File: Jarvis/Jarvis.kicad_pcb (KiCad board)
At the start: 4 copper layers, 30 x 55.1 mm, 134 parts, among them IC1 ADP1607, IC2 MAX-8Q, IC3 MPU-9250, IC4 STM32F411CxUx, IC5 Si4460, IC6 MS5611-01BA03, IC7 S25FL127S, J1 PYRO, J2 PWR, J3 ARM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

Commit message: Modified radio circuit to 868MHz and generated stickerBOM
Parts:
- C23: value 5.1pF -> 3pF
- C24: value 2.7pF -> 1.2pF
- C25: value 18pF -> 33pF
- C26, C28: value 8.2pF -> 5.1pF
- C27: value 15pF -> 10pF
- L2: value 56nH -> 18nH
- L3: value 56nH -> 22nH
- L4, L5: value 18nH -> 6.8nH
- L6: value 56nH -> 8.2nH
- L7: value 220nH -> 120nH
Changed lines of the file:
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@@
-(kicad_pcb (version 4) (host pcbnew 4.0.2-4+6225~38~ubuntu14.04.1-stable)
+(kicad_pcb (version 4) (host pcbnew 4.0.2+e4-6225~38~ubuntu14.04.1-stable)
   (general
-    (links 308)
-    (no_connects 0)
-    (area 81.675 72.611 117.344048 131.975)
+    (links 342)
+    (no_connects 24)
+    (area 84.924998 74.924999 115.075001 130.175002)
     (thickness 1.6)
     (drawings 164)
@@
     (45 Margin user hide)
     (46 B.CrtYd user hide)
-    (47 F.CrtYd user hide)
+    (47 F.CrtYd user)
     (48 B.Fab user hide)
     (49 F.Fab user hide)
@@
     (pad_to_mask_clearance 0)
     (aux_axis_origin 0 0)
-    (visible_elements FFFCDE1F)
+    (visible_elements FFFCCE1F)
     (pcbplotparams
       (layerselection 0x00030_80000001)
@@
       (effects (font (size 1 1) (thickness 0.15)))
     )
-    (fp_text value 5.1pF (at 1.61 0 270) (layer F.Fab)
+    (fp_text value 3pF (at 1.61 0 270) (layer F.Fab)
       (effects (font (size 1 1) (thickness 0.15)))
     )
@@
       (effects (font (size 1 1) (thickness 0.15)))
     )
-    (fp_text value 2.7pF (at 1.61 0 180) (layer F.Fab)
+    (fp_text value 1.2pF (at 1.61 0 180) (layer F.Fab)
       (effects (font (size 1 1) (thickness 0.15)))
     )
@@
       (effects (font (size 1 1) (thickness 0.15)))
     )
-    (fp_text value 18pF (at 1.61 0 180) (layer F.Fab)
+    (fp_text value 33pF (at 1.61 0 180) (layer F.Fab)
       (effects (font (size 1 1) (thickness 0.15)))
     )
@@
       (effects (font (size 1 1) (thickness 0.15)))
     )
-    (fp_text value 8.2pF (at 1.61 0 270) (layer F.Fab)
+    (fp_text value 5.1pF (at 1.61 0 270) (layer F.Fab)
       (effects (font (size 1 1) (thickness 0.15)))
     )
@@
       (effects (font (size 1 1) (thickness 0.15)))
     )
-    (fp_text value 15pF (at 1.61 0 90) (layer F.Fab)
+    (fp_text value 10pF (at 1.61 0 90) (layer F.Fab)
       (effects (font (size 1 1) (thickness 0.15)))
     )
@@
       (effects (font (size 1 1) (thickness 0.15)))
     )
-    (fp_text value 8.2pF (at 1.61 0 90) (layer F.Fab)
+    (fp_text value 5.1pF (at 1.61 0 90) (layer F.Fab)
       (effects (font (size 1 1) (thickness 0.15)))
     )
@@
       (effects (font (size 1 1) (thickness 0.15)))
     )
-    (fp_text value 56nH (at 1.61 0 90) (layer F.Fab)
+    (fp_text value 18nH (at 1.61 0 90) (layer F.Fab)
       (effects (font (size 1 1) (thickness 0.15)))
     )
@@
       (effects (font (size 1 1) (thickness 0.15)))
     )
-    (fp_text value 56nH (at 1.61 0 180) (layer F.Fab)
+    (fp_text value 22nH (at 1.61 0 180) (layer F.Fab)
       (effects (font (size 1 1) (thickness 0.15)))
     )
@@
       (effects (font (size 1 1) (thickness 0.15)))
     )
-    (fp_text value 18nH (at 1.61 0 90) (layer F.Fab)
+    (fp_text value 6.8nH (at 1.61 0 90) (layer F.Fab)
       (effects (font (size 1 1) (thickness 0.15)))
     )
@@
       (effects (font (size 1 1) (thickness 0.15)))
     )
-    (fp_text value 18nH (at 1.61 0 180) (layer F.Fab)
+    (fp_text value 6.8nH (at 1.61 0 180) (layer F.Fab)
       (effects (font (size 1 1) (thickness 0.15)))
     )
@@
       (effects (font (size 1 1) (thickness 0.15)))
     )
-    (fp_text value 56nH (at 1.61 0 180) (layer F.Fab)
+    (fp_text value 8.2nH (at 1.61 0 180) (layer F.Fab)
       (effects (font (size 1 1) (thickness 0.15)))
     )
@@
       (effects (font (size 1 1) (thickness 0.15)))
     )
-    (fp_text value 220nH (at 2.025 0 270) (layer F.Fab)
+    (fp_text value 120nH (at 2.025 0 270) (layer F.Fab)
       (effects (font (size 1 1) (thickness 0.15)))
     )

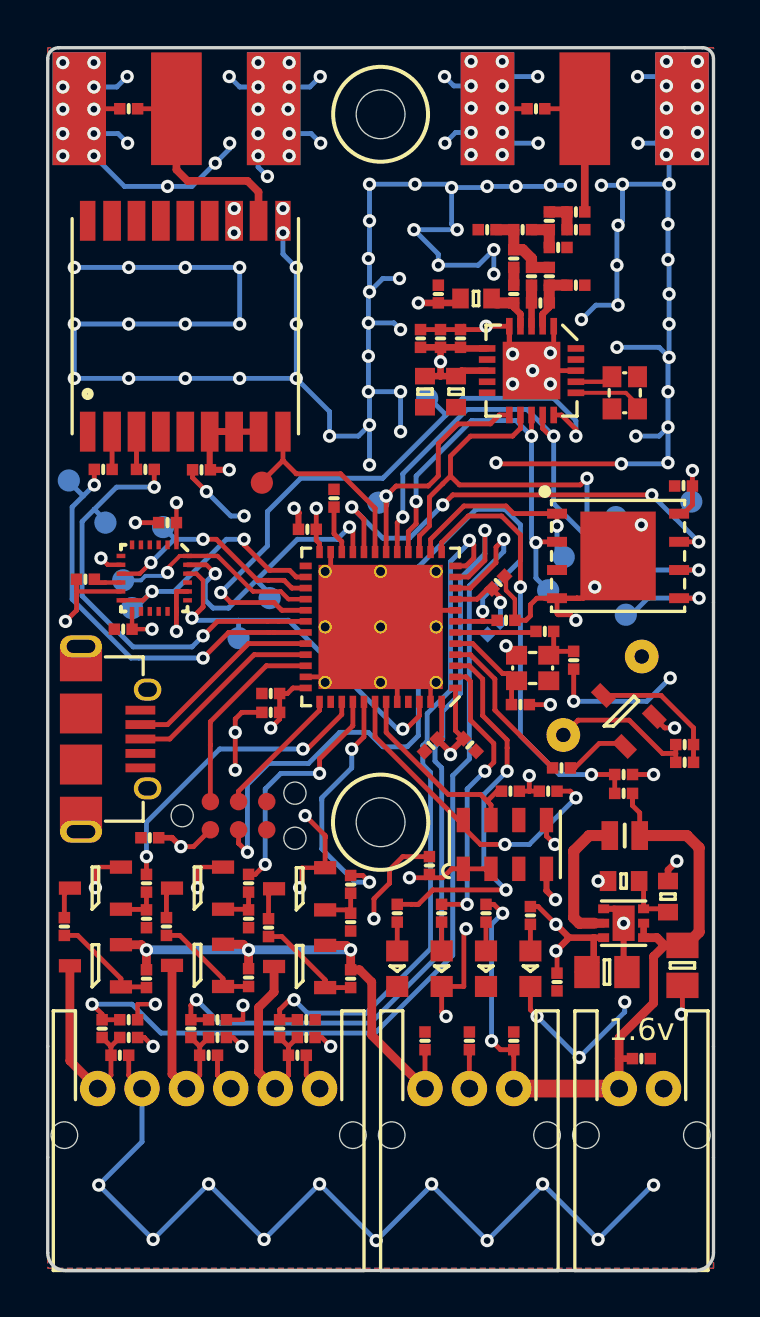
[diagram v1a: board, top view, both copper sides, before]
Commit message: Corrected Radio Passives in Ground Station
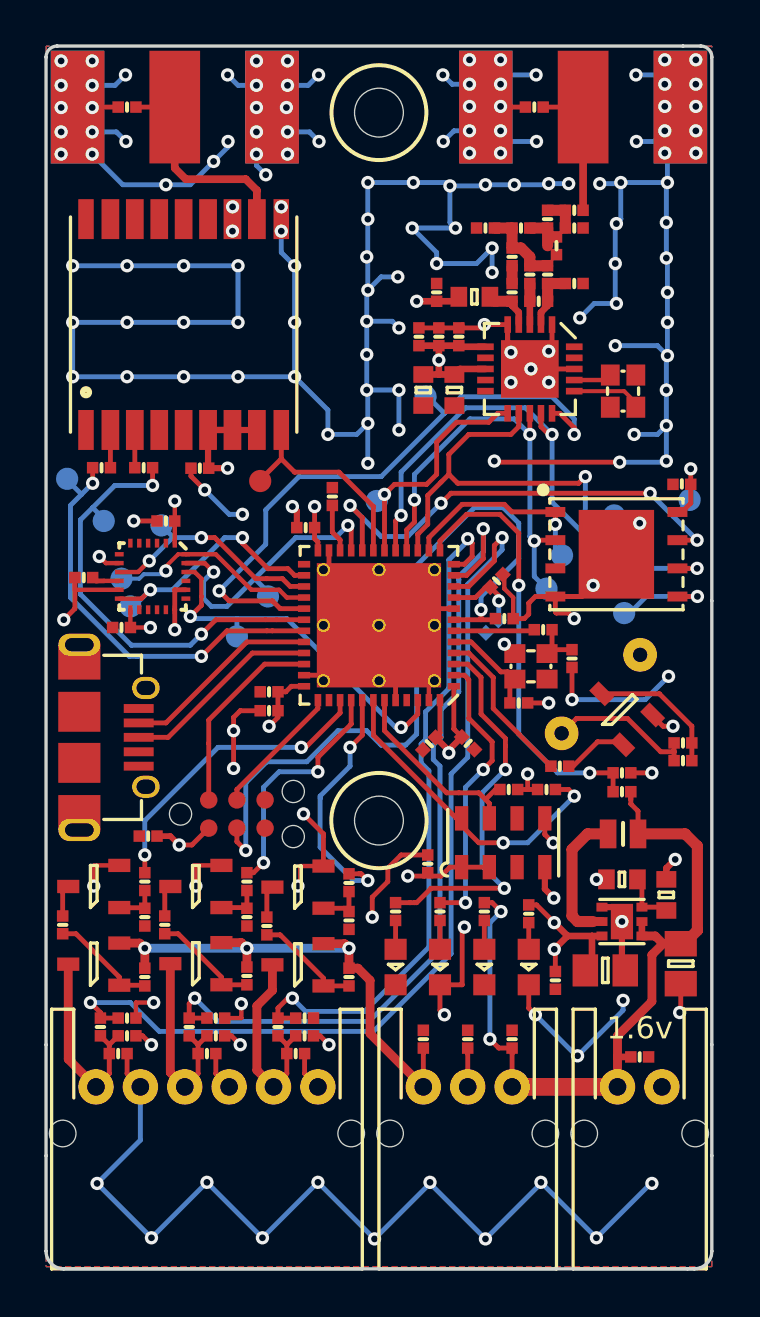
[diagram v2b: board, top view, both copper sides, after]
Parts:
- moved C1 0.11 mm to (91.9, 93.9)
- moved C10 0.11 mm to (88.3, 101.1)
- moved C11 0.11 mm to (90.3, 96.3)
- moved C12 0.11 mm to (96.6, 96.6)
- moved C13 0.11 mm to (103.9, 106.3)
- moved C15 0.11 mm to (86.6, 98.9)
- moved C19 0.11 mm to (97.8, 95.2)
- moved C20 0.11 mm to (105.6, 100.7)
- moved C21 0.11 mm to (106.2, 104.5)
- moved C23 0.11 mm to (108.7, 85.6)
- moved C24 0.11 mm to (106.7, 85.2)
- moved C26 0.11 mm to (104.7, 83.1)
- moved C27 0.11 mm to (107.9, 83.9), turned to 270 degrees
- moved C28 0.11 mm to (108.7, 83.1)
- moved C29 0.11 mm to (113.6, 94.7)
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
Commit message: Tidy up before final assembly
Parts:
- turned C27 to 0 degrees
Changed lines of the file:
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@@
 (kicad_pcb (version 4) (host pcbnew 4.0.2+e4-6225~38~ubuntu14.04.1-stable)
   (general
-    (links 308)
-    (no_connects 0)
-    (area 69.827524 81.909999 129.191524 119.977524)
+    (links 342)
+    (no_connects 24)
+    (area 84.849998 74.849999 115.000001 130.100002)
     (thickness 1.6)
     (drawings 164)
@@
   )
   (module agg:0402-L (layer F.Cu)
-    (at 107.925 83.925 270)
-    (fp_text reference C27 (at -1.61 0 360) (layer F.Fab)
-      (effects (font (size 1 1) (thickness 0.15)))
-    )
-    (fp_text value 10pF (at 1.61 0 360) (layer F.Fab)
-      (effects (font (size 1 1) (thickness 0.15)))
-    )
-    (fp_line (start -0.5 -0.25) (end 0.5 -0.25) (layer F.Fab) (width 0.01))
-    (fp_line (start 0.5 -0.25) (end 0.5 0.25) (layer F.Fab) (width 0.01))
-    (fp_line (start 0.5 0.25) (end -0.5 0.25) (layer F.Fab) (width 0.01))
-    (fp_line (start -0.5 0.25) (end -0.5 -0.25) (layer F.Fab) (width 0.01))
-    (fp_line (start -0.2 -0.25) (end -0.2 0.25) (layer F.Fab) (width 0.01))
-    (fp_line (start 0.2 -0.25) (end 0.2 0.25) (layer F.Fab) (width 0.01))
-    (fp_line (start -0.8 -0.4) (end 0.8 -0.4) (layer F.CrtYd) (width 0.01))
-    (fp_line (start 0.8 -0.4) (end 0.8 0.4) (layer F.CrtYd) (width 0.01))
-    (fp_line (start 0.8 0.4) (end -0.8 0.4) (layer F.CrtYd) (width 0.01))
-    (fp_line (start -0.8 0.4) (end -0.8 -0.4) (layer F.CrtYd) (width 0.01))
-    (pad 1 smd rect (at -0.4 0 270) (size 0.52 0.52) (layers F.Cu F.Paste F.Mask)
+    (at 107.925 83.925)
+    (fp_text reference C27 (at -1.61 0 90) (layer F.Fab)
+      (effects (font (size 1 1) (thickness 0.15)))
+    )
+    (fp_text value 10pF (at 1.61 0 90) (layer F.Fab)
+      (effects (font (size 1 1) (thickness 0.15)))
+    )
+    (fp_line (start -0.5 -0.25) (end 0.5 -0.25) (layer F.Fab) (width 0.01))
+    (fp_line (start 0.5 -0.25) (end 0.5 0.25) (layer F.Fab) (width 0.01))
+    (fp_line (start 0.5 0.25) (end -0.5 0.25) (layer F.Fab) (width 0.01))
+    (fp_line (start -0.5 0.25) (end -0.5 -0.25) (layer F.Fab) (width 0.01))
+    (fp_line (start -0.2 -0.25) (end -0.2 0.25) (layer F.Fab) (width 0.01))
+    (fp_line (start 0.2 -0.25) (end 0.2 0.25) (layer F.Fab) (width 0.01))
+    (fp_line (start -0.8 -0.4) (end 0.8 -0.4) (layer F.CrtYd) (width 0.01))
+    (fp_line (start 0.8 -0.4) (end 0.8 0.4) (layer F.CrtYd) (width 0.01))
+    (fp_line (start 0.8 0.4) (end -0.8 0.4) (layer F.CrtYd) (width 0.01))
+    (fp_line (start -0.8 0.4) (end -0.8 -0.4) (layer F.CrtYd) (width 0.01))
+    (pad 1 smd rect (at -0.4 0) (size 0.52 0.52) (layers F.Cu F.Paste F.Mask)
       (net 44 "Net-(C27-Pad1)"))
-    (pad 2 smd rect (at 0.4 0 270) (size 0.52 0.52) (layers F.Cu F.Paste F.Mask)
-      (net 2 GND))
-  )
+    (pad 2 smd rect (at 0.4 0) (size 0.52 0.52) (layers F.Cu F.Paste F.Mask)
+      (net 2 GND))
+  )
